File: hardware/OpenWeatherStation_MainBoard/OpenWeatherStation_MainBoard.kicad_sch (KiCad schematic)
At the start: 0 parts

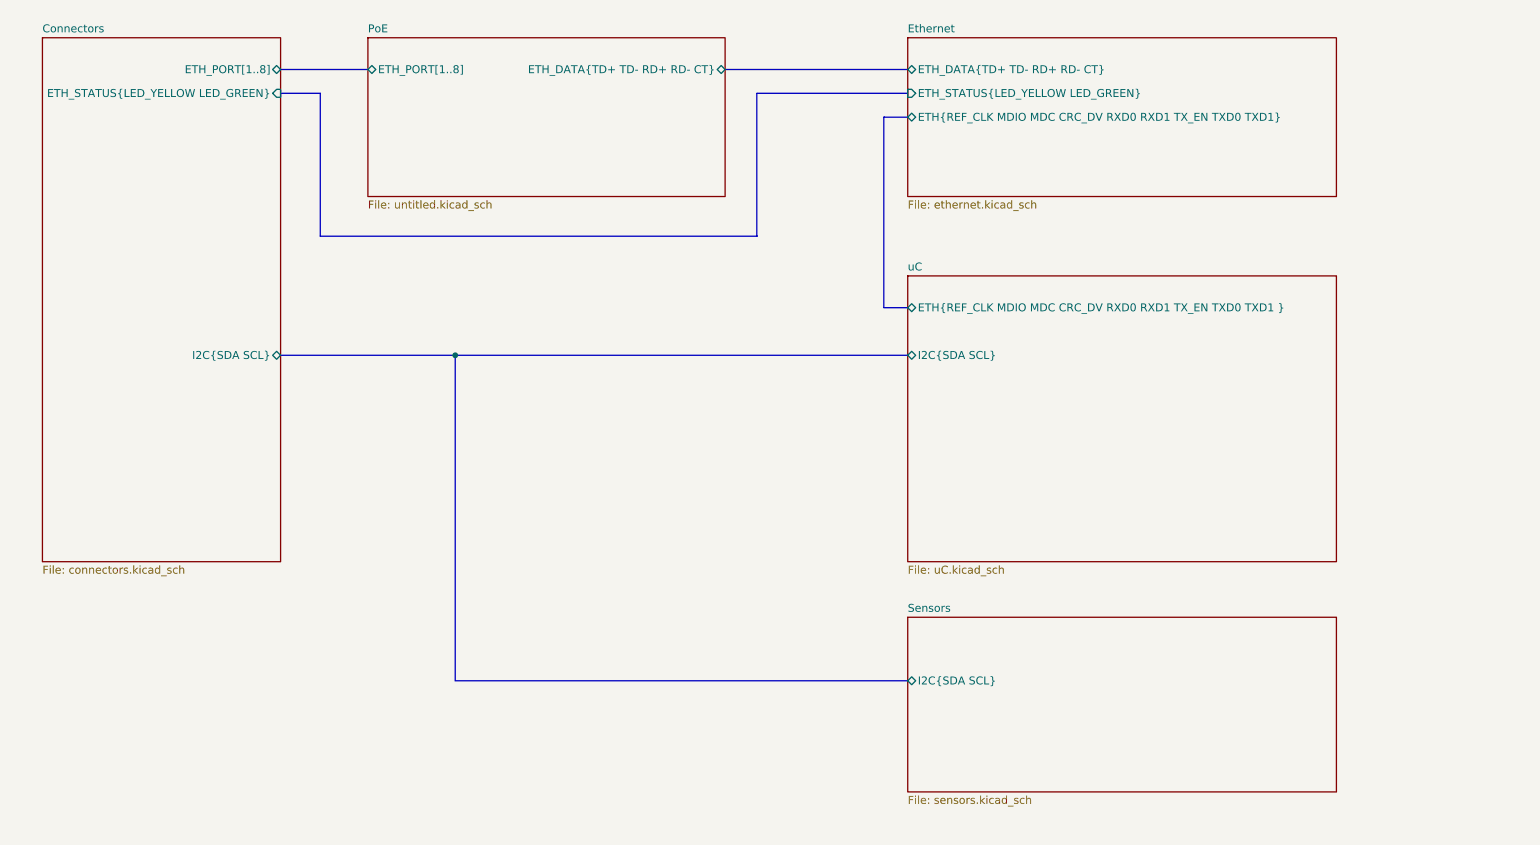
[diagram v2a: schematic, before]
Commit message: update schematic
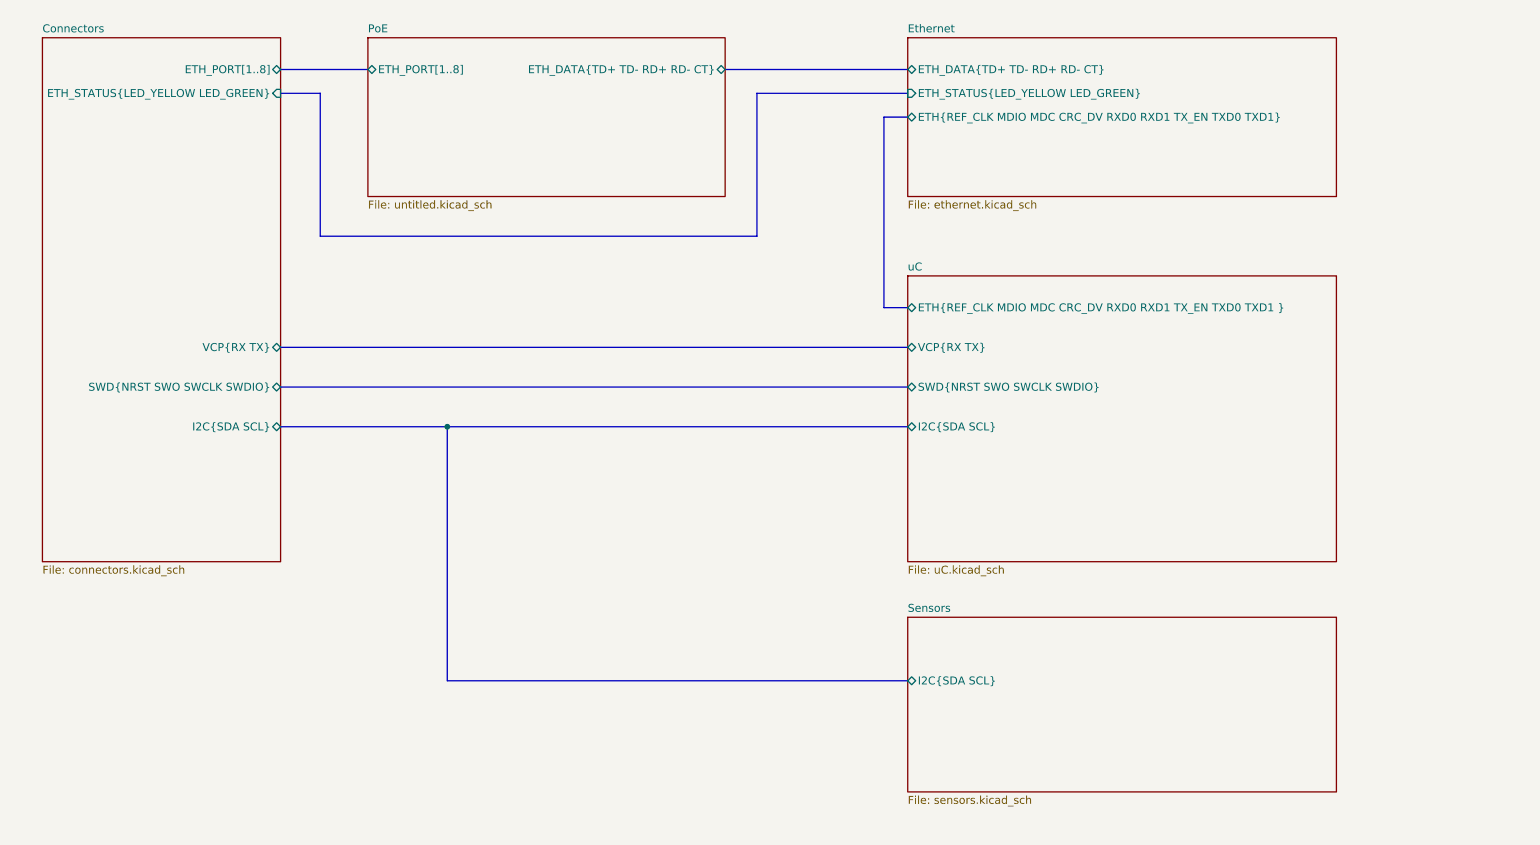
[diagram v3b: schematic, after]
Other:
- sheet Connectors ports: added SWD{NRST SWO SWCLK SWDIO}, VCP{RX TX}; removed none
- sheet uC ports: added SWD{NRST SWO SWCLK SWDIO}, VCP{RX TX}; removed none
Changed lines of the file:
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@@
 (kicad_sch (version 20230121) (generator eeschema)
   (paper "A4")
-  (junction (at 82.55 82.55) (diameter 0) (color 0 0 0 0)
-  )
-  (bus (pts (xy 82.55 82.55) (xy 82.55 134.62))
-    (stroke (width 0) (type default))
-  )
-  (bus (pts (xy 54.61 82.55) (xy 82.55 82.55))
-    (stroke (width 0) (type default))
+  (junction (at 81.28 93.98) (diameter 0) (color 0 0 0 0)
   )
   (bus (pts (xy 60.96 63.5) (xy 130.81 63.5))
     (stroke (width 0) (type default))
   )
+  (bus (pts (xy 81.28 93.98) (xy 81.28 134.62))
+    (stroke (width 0) (type default))
+  )
   (bus (pts (xy 151.13 44.45) (xy 151.13 74.93))
+    (stroke (width 0) (type default))
+  )
+  (bus (pts (xy 54.61 87.63) (xy 154.94 87.63))
     (stroke (width 0) (type default))
   )
@@
     (stroke (width 0) (type default))
   )
-  (bus (pts (xy 82.55 134.62) (xy 154.94 134.62))
+  (bus (pts (xy 81.28 134.62) (xy 154.94 134.62))
     (stroke (width 0) (type default))
   )
@@
     (stroke (width 0) (type default))
   )
+  (bus (pts (xy 154.94 81.28) (xy 54.61 81.28))
+    (stroke (width 0) (type default))
+  )
   (bus (pts (xy 60.96 40.64) (xy 60.96 63.5))
     (stroke (width 0) (type default))
   )
-  (bus (pts (xy 154.94 82.55) (xy 82.55 82.55))
+  (bus (pts (xy 54.61 93.98) (xy 81.28 93.98))
+    (stroke (width 0) (type default))
+  )
+  (bus (pts (xy 154.94 93.98) (xy 81.28 93.98))
     (stroke (width 0) (type default))
   )
@@
       (effects (font (size 1.27 1.27)) (justify left top))
     )
-    (pin "I2C{SDA SCL}" bidirectional (at 54.61 82.55 0)
+    (pin "I2C{SDA SCL}" bidirectional (at 54.61 93.98 0)
       (effects (font (size 1.27 1.27)) (justify right))
     )
@@
     )
     (pin "ETH_STATUS{LED_YELLOW LED_GREEN}" input (at 54.61 40.64 0)
+      (effects (font (size 1.27 1.27)) (justify right))
+    )
+    (pin "VCP{RX TX}" bidirectional (at 54.61 81.28 0)
+      (effects (font (size 1.27 1.27)) (justify right))
+    )
+    (pin "SWD{NRST SWO SWCLK SWDIO}" bidirectional (at 54.61 87.63 0)
       (effects (font (size 1.27 1.27)) (justify right))
     )
@@
       (effects (font (size 1.27 1.27)) (justify left top))
     )
-    (pin "I2C{SDA SCL}" bidirectional (at 154.94 82.55 180)
+    (pin "I2C{SDA SCL}" bidirectional (at 154.94 93.98 180)
       (effects (font (size 1.27 1.27)) (justify left))
     )
@@
       (effects (font (size 1.27 1.27)) (justify left))
     )
+    (pin "VCP{RX TX}" bidirectional (at 154.94 81.28 180)
+      (effects (font (size 1.27 1.27)) (justify left))
+    )
+    (pin "SWD{NRST SWO SWCLK SWDIO}" bidirectional (at 154.94 87.63 180)
+      (effects (font (size 1.27 1.27)) (justify left))
+    )

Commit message: schematic update
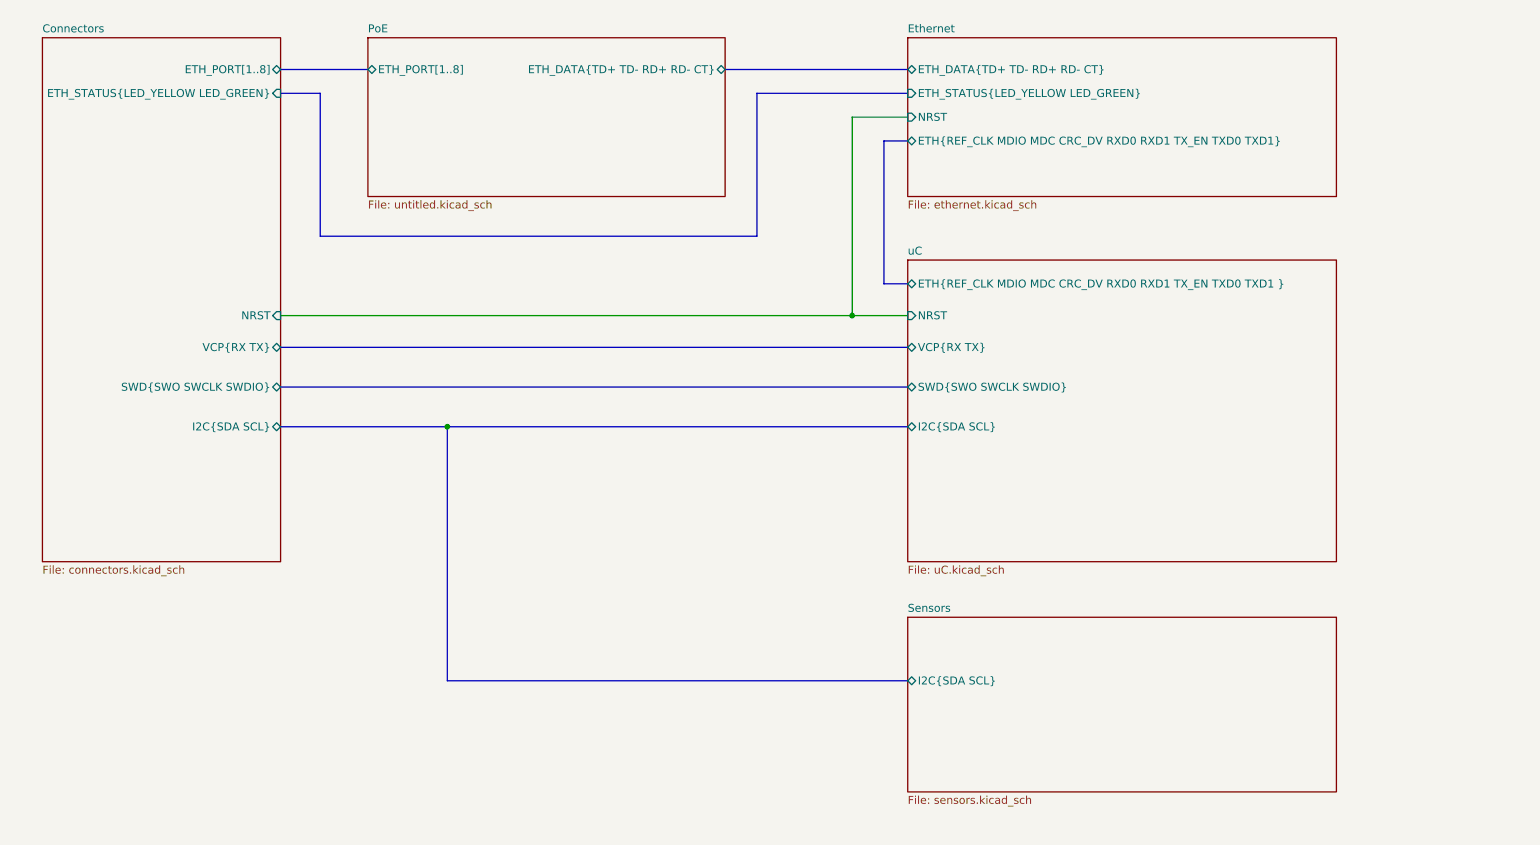
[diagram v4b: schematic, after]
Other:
- sheet Connectors ports: added NRST, SWD{SWO SWCLK SWDIO}; removed SWD{NRST SWO SWCLK SWDIO}
- sheet Ethernet ports: added NRST; removed none
- sheet uC ports: added NRST, SWD{SWO SWCLK SWDIO}; removed SWD{NRST SWO SWCLK SWDIO}
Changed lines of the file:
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@@
   (junction (at 81.28 93.98) (diameter 0) (color 0 0 0 0)
+  )
+  (junction (at 146.05 76.2) (diameter 0) (color 0 0 0 0)
   )
   (bus (pts (xy 60.96 63.5) (xy 130.81 63.5))
@@
     (stroke (width 0) (type default))
   )
-  (bus (pts (xy 151.13 44.45) (xy 151.13 74.93))
+  (bus (pts (xy 151.13 48.26) (xy 151.13 71.12))
+    (stroke (width 0) (type default))
+  )
+  (wire (pts (xy 146.05 44.45) (xy 146.05 76.2))
+    (stroke (width 0) (type default))
+  )
+  (wire (pts (xy 154.94 44.45) (xy 146.05 44.45))
+    (stroke (width 0) (type default))
+  )
+  (wire (pts (xy 54.61 76.2) (xy 146.05 76.2))
     (stroke (width 0) (type default))
   )
@@
     (stroke (width 0) (type default))
   )
-  (bus (pts (xy 154.94 44.45) (xy 151.13 44.45))
+  (bus (pts (xy 154.94 48.26) (xy 151.13 48.26))
     (stroke (width 0) (type default))
   )
@@
     (stroke (width 0) (type default))
   )
-  (bus (pts (xy 151.13 74.93) (xy 154.94 74.93))
+  (bus (pts (xy 151.13 71.12) (xy 154.94 71.12))
+    (stroke (width 0) (type default))
+  )
+  (wire (pts (xy 146.05 76.2) (xy 154.94 76.2))
     (stroke (width 0) (type default))
   )
@@
       (effects (font (size 1.27 1.27)) (justify left))
     )
-    (pin "ETH{REF_CLK MDIO MDC CRC_DV RXD0 RXD1 TX_EN TXD0 TXD1}" bidirectional (at 154.94 44.45 180)
+    (pin "ETH{REF_CLK MDIO MDC CRC_DV RXD0 RXD1 TX_EN TXD0 TXD1}" bidirectional (at 154.94 48.26 180)
+      (effects (font (size 1.27 1.27)) (justify left))
+    )
+    (pin "NRST" input (at 154.94 44.45 180)
       (effects (font (size 1.27 1.27)) (justify left))
     )
@@
       (effects (font (size 1.27 1.27)) (justify right))
     )
-    (pin "SWD{NRST SWO SWCLK SWDIO}" bidirectional (at 54.61 87.63 0)
+    (pin "NRST" input (at 54.61 76.2 0)
+      (effects (font (size 1.27 1.27)) (justify right))
+    )
+    (pin "SWD{SWO SWCLK SWDIO}" bidirectional (at 54.61 87.63 0)
       (effects (font (size 1.27 1.27)) (justify right))
     )
@@
     )
   )
-  (sheet (at 154.94 69.85) (size 68.58 45.72) (fields_autoplaced)
+  (sheet (at 154.94 67.31) (size 68.58 48.26) (fields_autoplaced)
     (stroke (width 0.1524) (type solid))
     (fill (color 0 0 0 0.0000))
-    (property "Sheetname" "uC" (at 154.94 69.1384 0)
+    (property "Sheetname" "uC" (at 154.94 66.5984 0)
       (effects (font (size 1.27 1.27)) (justify left bottom))
     )
@@
       (effects (font (size 1.27 1.27)) (justify left))
     )
-    (pin "ETH{REF_CLK MDIO MDC CRC_DV RXD0 RXD1 TX_EN TXD0 TXD1 }" bidirectional (at 154.94 74.93 180)
+    (pin "ETH{REF_CLK MDIO MDC CRC_DV RXD0 RXD1 TX_EN TXD0 TXD1 }" bidirectional (at 154.94 71.12 180)
       (effects (font (size 1.27 1.27)) (justify left))
     )
@@
       (effects (font (size 1.27 1.27)) (justify left))
     )
-    (pin "SWD{NRST SWO SWCLK SWDIO}" bidirectional (at 154.94 87.63 180)
+    (pin "NRST" input (at 154.94 76.2 180)
       (effects (font (size 1.27 1.27)) (justify left))
     )
+    (pin "SWD{SWO SWCLK SWDIO}" bidirectional (at 154.94 87.63 180)
+      (effects (font (size 1.27 1.27)) (justify left))
+    )
